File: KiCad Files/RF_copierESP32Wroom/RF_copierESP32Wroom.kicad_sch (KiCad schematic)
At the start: 45 parts, among them J1 USB_B_Micro, Q1 S8050, Q2 S8050, SW1 SW Boot Option, SW2 SW Boot Option, SW3 UP, SW4 DOWN, SW5 LEFT, SW6 RIGHT, U1 ESP32-WROOM-32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

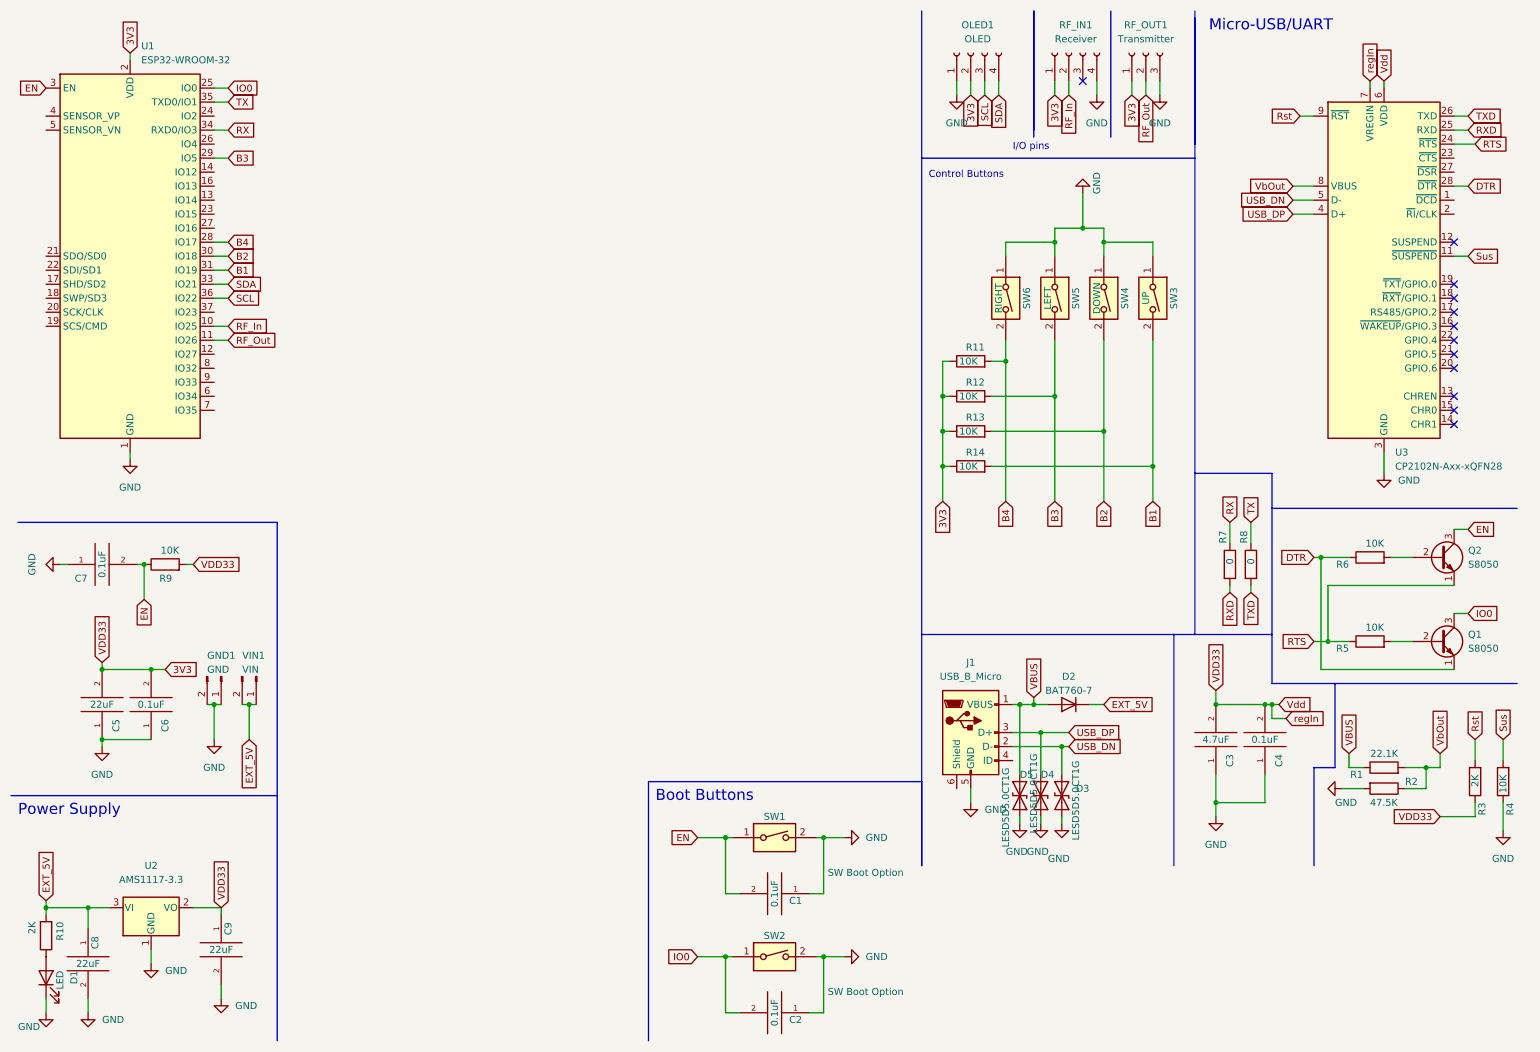
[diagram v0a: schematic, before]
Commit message: added bettery charger and footprints
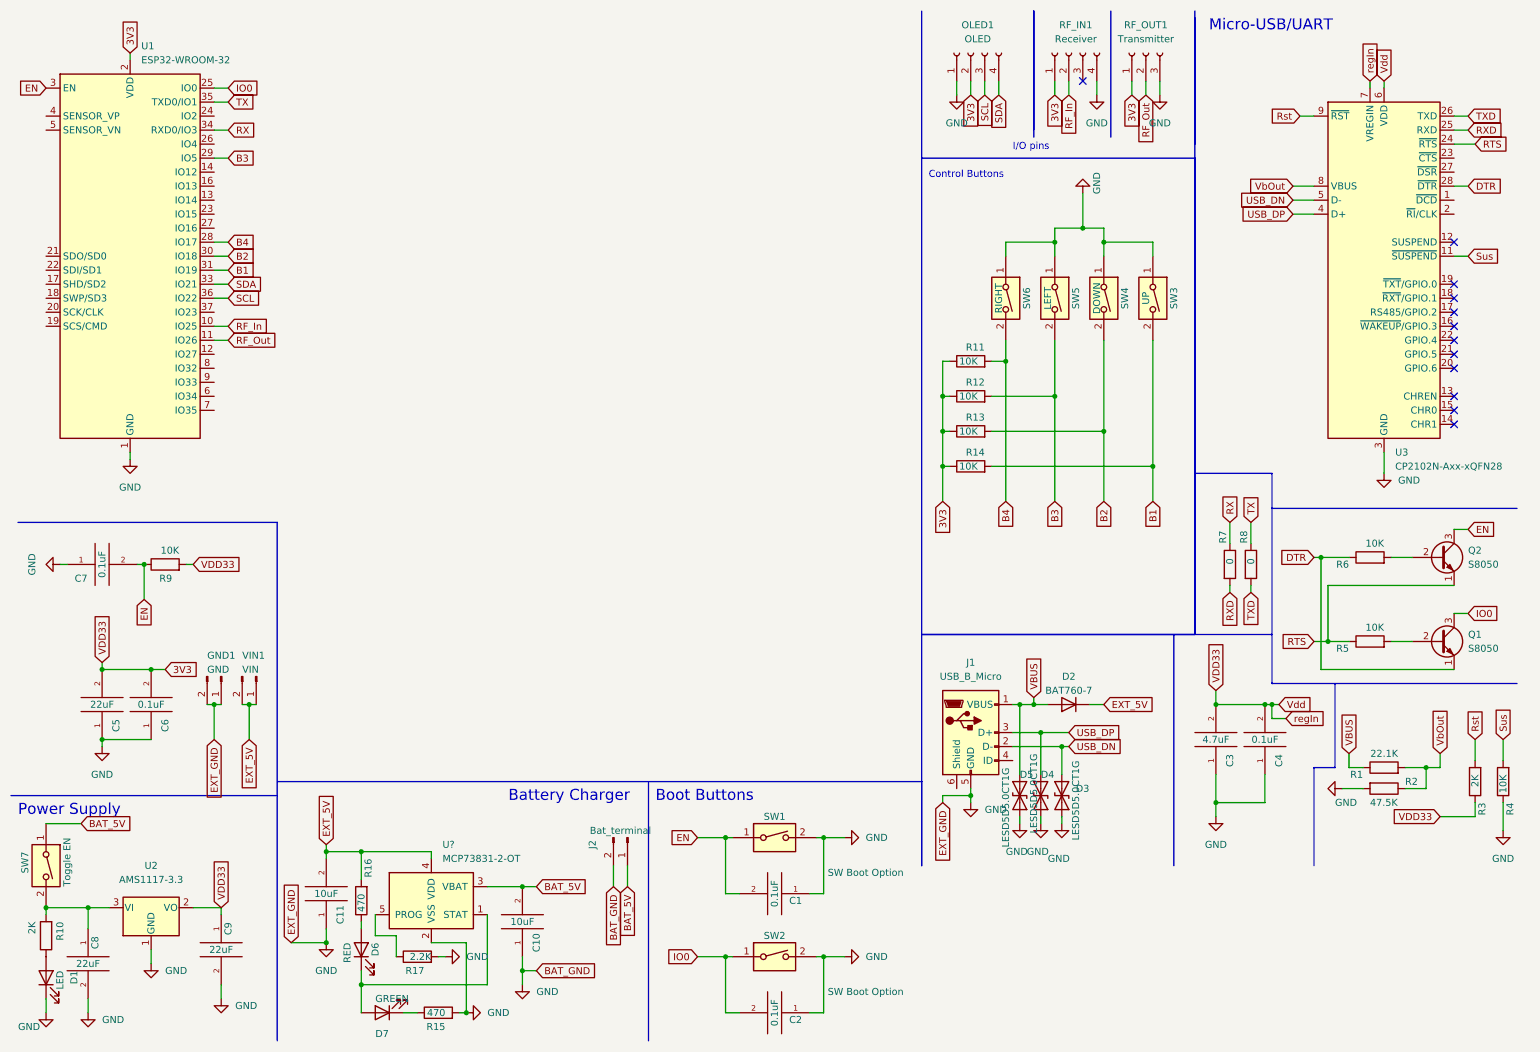
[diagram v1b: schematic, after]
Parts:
- added C10, C11: 10uF, Capacitor_SMD:C_0201_0603Metric_Pad0.64x0.40mm_HandSolder, symbol pspice:CAP
- added D6: RED, Diode_SMD:D_1206_3216Metric_Pad1.42x1.75mm_HandSolder, symbol Device:LED
- added D7: GREEN, Diode_SMD:D_1206_3216Metric_Pad1.42x1.75mm_HandSolder, symbol Device:LED
- added J2: Bat_terminal, Connector_JST:JST_PH_S2B-PH-K_1x02_P2.00mm_Horizontal, symbol Connector:Conn_01x02_Male
- added R15, R16: 470, Resistor_SMD:R_0201_0603Metric, symbol Device:R
- added R17: 2.2K, Resistor_SMD:R_0201_0603Metric, symbol Device:R
- added SW7: Toggle EN, symbol Switch:SW_DIP_x01
- added U?: MCP73831-2-OT, Package_TO_SOT_SMD:SOT-23-5, symbol Battery_Management:MCP73831-2-OT
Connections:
- net EXT_5V: now also C11.2, R16.2, U?.4 (VDD); no longer C8.1, R10.2, U2.3 (VI)
- net GND: now also C10.1, C11.1, J2.2 (Pin_2), R15.2, R17.2, U?.2 (VSS)
- new net: D7.1 (K), R15.1
- new net: D6.1 (K), D7.2 (A), U?.1 (STAT)
- new net: D6.2 (A), R16.1
- new net: R17.1, U?.5 (PROG)
- new net: C8.1, R10.2, SW7.2, U2.3 (VI)
- new net BAT_5V: C10.2, J2.1 (Pin_1), SW7.1, U?.3 (VBAT)
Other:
- note added: "Battery Charger"
